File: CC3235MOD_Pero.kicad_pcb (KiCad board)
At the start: 2 copper layers, 37 parts, among them J1 USB_B_Mini, J2 JTAG/SWD, SW1 Reset, SW2 SW_DIP_x03, SW3 User IO, U1 TLV1117-33, U2 CP2102N-A01-GQFN24, U3 CC3235MODSF12MOBR

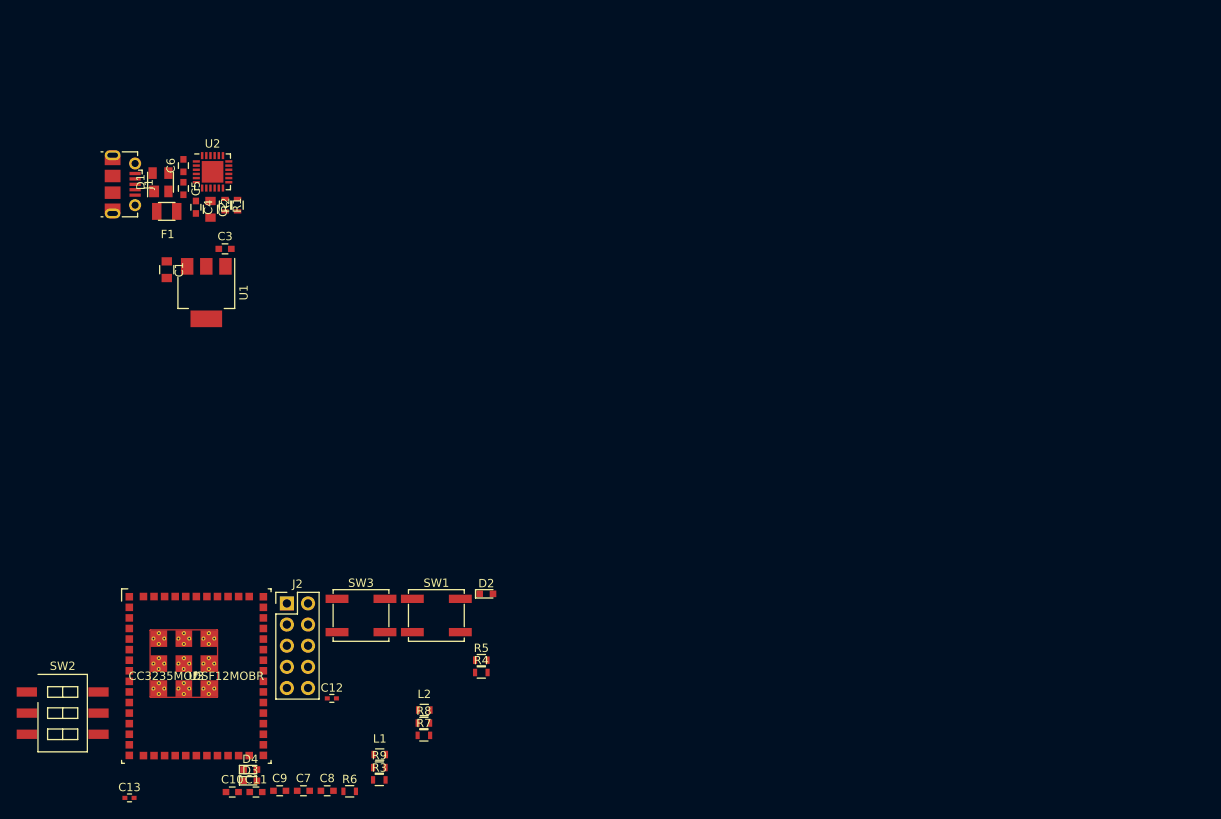
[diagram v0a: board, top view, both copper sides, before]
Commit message: antenna footprint done
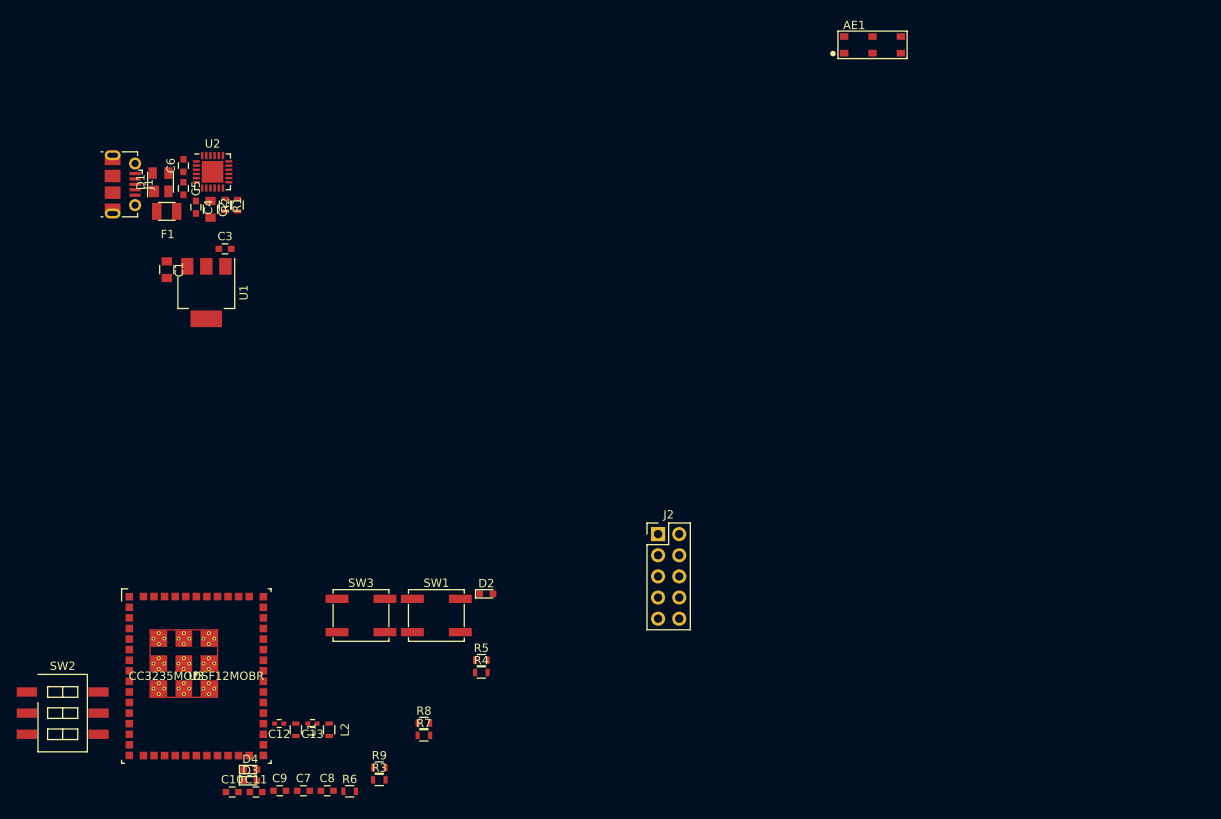
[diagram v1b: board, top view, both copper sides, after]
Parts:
- added AE1: Antenna, footprints:M830520, F.Cu at (148.8, 52.8)
- moved J2 45.3 mm to (123.0, 111.5)
- moved C13 23.7 mm to (81.5, 134.2), turned to 180 degrees
- moved L2 11.7 mm to (83.5, 135.0), turned to 270 degrees
- moved L1 10.5 mm to (79.5, 135.0), turned to 270 degrees
- moved C12 7.01 mm to (77.5, 134.2), turned to 180 degrees
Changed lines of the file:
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@@
     (tracks 0)
     (zones 0)
-    (modules 37)
+    (modules 38)
     (nets 72)
   )
@@
     (pad_to_mask_clearance 0.2)
     (aux_axis_origin 0 0)
-    (visible_elements FFFFFFFF)
+    (visible_elements 7FFFFFFF)
     (pcbplotparams
       (layerselection 0x010fc_ffffffff)
@@
     (add_net VBUS)
   )
+  (module footprints:M830520 (layer F.Cu)
+    (at 148.75 52.75)
+    (fp_text reference AE1 (at -2.2 -2.35) (layer F.SilkS)
+      (effects (font (size 1 1) (thickness 0.15)))
+    )
+    (fp_text value Antenna (at 0.7 2.5) (layer F.Fab)
+      (effects (font (size 1 1) (thickness 0.15)))
+    )
+    (fp_line (start -4 -1.5) (end 4 -1.5) (layer F.CrtYd) (width 0.1))
+    (fp_line (start 4 -1.5) (end 4 1.5) (layer F.CrtYd) (width 0.1))
+    (fp_line (start 4 1.5) (end -4 1.5) (layer F.CrtYd) (width 0.1))
+    (fp_line (start -4 1.5) (end -4 -1.5) (layer F.CrtYd) (width 0.1))
+    (fp_line (start -4.15 -1.65) (end 4.15 -1.65) (layer F.SilkS) (width 0.15))
+    (fp_line (start 4.15 -1.65) (end 4.15 1.6) (layer F.SilkS) (width 0.15))
+    (fp_line (start 4.15 1.6) (end 4.15 1.65) (layer F.SilkS) (width 0.15))
+    (fp_line (start 4.15 1.65) (end -4.15 1.65) (layer F.SilkS) (width 0.15))
+    (fp_line (start -4.15 1.65) (end -4.15 -1.65) (layer F.SilkS) (width 0.15))
+    (fp_circle (center -4.75 1.05) (end -4.5 1.05) (layer F.SilkS) (width 0.15))
+    (fp_circle (center -4.75 1.05) (end -4.65 1.05) (layer F.SilkS) (width 0.15))
+    (pad 1 smd rect (at -3.4 1) (size 1 0.8) (layers F.Cu F.Paste F.Mask)
+      (net 1 GND))
+    (pad 2 smd rect (at -3.4 -1) (size 1 0.8) (layers F.Cu F.Paste F.Mask)
+      (net 53 "Net-(AE1-Pad2)"))
+    (pad 3 smd rect (at 0 -1) (size 1 0.8) (layers F.Cu F.Paste F.Mask))
+    (pad 4 smd rect (at 3.4 -1) (size 1 0.8) (layers F.Cu F.Paste F.Mask))
+    (pad 5 smd rect (at 3.4 1) (size 1 0.8) (layers F.Cu F.Paste F.Mask))
+    (pad 6 smd rect (at 0 1) (size 1 0.8) (layers F.Cu F.Paste F.Mask))
+  )
   (module TO_SOT_Packages_SMD:SOT-143 (layer F.Cu)
     (at 63.25 69.25 90)
@@
   )
   (module Capacitors_SMD:C_0402 (layer F.Cu)
-    (at 59.525001 143.180001)
+    (at 81.5 134.25 180)
     (descr "Capacitor SMD 0402, reflow soldering, AVX (see smccp.pdf)")
     (tags "capacitor 0402")
     (attr smd)
-    (fp_text reference C13 (at 0 -1.27) (layer F.SilkS)
-      (effects (font (size 1 1) (thickness 0.15)))
-    )
-    (fp_text value C (at 0 1.27) (layer F.Fab)
-      (effects (font (size 1 1) (thickness 0.15)))
-    )
-    (fp_text user %R (at 0 -1.27) (layer F.Fab)
+    (fp_text reference C13 (at 0 -1.27 180) (layer F.SilkS)
+      (effects (font (size 1 1) (thickness 0.15)))
+    )
+    (fp_text value C (at 0 1.27 180) (layer F.Fab)
+      (effects (font (size 1 1) (thickness 0.15)))
+    )
+    (fp_text user %R (at 0 -1.27 180) (layer F.Fab)
       (effects (font (size 1 1) (thickness 0.15)))
     )
@@
     (fp_line (start 1 0.4) (end 1 -0.4) (layer F.CrtYd) (width 0.05))
     (fp_line (start 1 0.4) (end -1 0.4) (layer F.CrtYd) (width 0.05))
-    (pad 1 smd rect (at -0.55 0) (size 0.6 0.5) (layers F.Cu F.Paste F.Mask)
+    (pad 1 smd rect (at -0.55 0 180) (size 0.6 0.5) (layers F.Cu F.Paste F.Mask)
       (net 53 "Net-(AE1-Pad2)"))
-    (pad 2 smd rect (at 0.55 0) (size 0.6 0.5) (layers F.Cu F.Paste F.Mask)
+    (pad 2 smd rect (at 0.55 0 180) (size 0.6 0.5) (layers F.Cu F.Paste F.Mask)
       (net 54 "Net-(C12-Pad1)"))
     (model Capacitors_SMD.3dshapes/C_0402.wrl
@@
   )
   (module Capacitors_SMD:C_0402 (layer F.Cu)
-    (at 83.825001 131.230001)
+    (at 77.5 134.25 180)
     (descr "Capacitor SMD 0402, reflow soldering, AVX (see smccp.pdf)")
     (tags "capacitor 0402")
     (attr smd)
-    (fp_text reference C12 (at 0 -1.27) (layer F.SilkS)
-      (effects (font (size 1 1) (thickness 0.15)))
-    )
-    (fp_text value C (at 0 1.27) (layer F.Fab)
+    (fp_text reference C12 (at 0 -1.27 180) (layer F.SilkS)
+      (effects (font (size 1 1) (thickness 0.15)))
+    )
+    (fp_text value C (at 0 1.27 180) (layer F.Fab)
       (effects (font (size 1 1) (thickness 0.15)))
     )
@@
     (fp_line (start 0.5 0.25) (end -0.5 0.25) (layer F.Fab) (width 0.1))
     (fp_line (start -0.5 0.25) (end -0.5 -0.25) (layer F.Fab) (width 0.1))
-    (fp_text user %R (at 0 -1.27) (layer F.Fab)
-      (effects (font (size 1 1) (thickness 0.15)))
-    )
-    (pad 2 smd rect (at 0.55 0) (size 0.6 0.5) (layers F.Cu F.Paste F.Mask)
+    (fp_text user %R (at 0 -1.27 180) (layer F.Fab)
+      (effects (font (size 1 1) (thickness 0.15)))
+    )
+    (pad 2 smd rect (at 0.55 0 180) (size 0.6 0.5) (layers F.Cu F.Paste F.Mask)
       (net 23 /RF_OUT))
-    (pad 1 smd rect (at -0.55 0) (size 0.6 0.5) (layers F.Cu F.Paste F.Mask)
+    (pad 1 smd rect (at -0.55 0 180) (size 0.6 0.5) (layers F.Cu F.Paste F.Mask)
       (net 54 "Net-(C12-Pad1)"))
     (model Capacitors_SMD.3dshapes/C_0402.wrl
@@
   )
   (module Inductors_SMD:L_0603 (layer F.Cu)
-    (at 89.575001 137.975001)
+    (at 79.5 135 270)
     (descr "Resistor SMD 0603, reflow soldering, Vishay (see dcrcw.pdf)")
     (tags "resistor 0603")
     (attr smd)
-    (fp_text reference L1 (at 0 -1.9) (layer F.SilkS)
-      (effects (font (size 1 1) (thickness 0.15)))
-    )
-    (fp_text value L (at 0 1.9) (layer F.Fab)
-      (effects (font (size 1 1) (thickness 0.15)))
-    )
-    (fp_text user %R (at 0 0) (layer F.Fab)
+    (fp_text reference L1 (at 0 -1.9 270) (layer F.SilkS)
+      (effects (font (size 1 1) (thickness 0.15)))
+    )
+    (fp_text value L (at 0 1.9 270) (layer F.Fab)
+      (effects (font (size 1 1) (thickness 0.15)))
+    )
+    (fp_text user %R (at 0 0 270) (layer F.Fab)
       (effects (font (size 0.4 0.4) (thickness 0.075)))
     )
@@
     (fp_line (start 0.5 0.68) (end -0.5 0.68) (layer F.SilkS) (width 0.12))
     (fp_line (start -0.5 -0.68) (end 0.5 -0.68) (layer F.SilkS) (width 0.12))
-    (pad 1 smd rect (at -0.75 0) (size 0.5 0.9) (layers F.Cu F.Paste F.Mask)
+    (pad 1 smd rect (at -0.75 0 270) (size 0.5 0.9) (layers F.Cu F.Paste F.Mask)
       (net 54 "Net-(C12-Pad1)"))
-    (pad 2 smd rect (at 0.75 0) (size 0.5 0.9) (layers F.Cu F.Paste F.Mask)
+    (pad 2 smd rect (at 0.75 0 270) (size 0.5 0.9) (layers F.Cu F.Paste F.Mask)
       (net 1 GND))
     (model ${KISYS3DMOD}/Inductors_SMD.3dshapes/L_0603.wrl
@@
   )
   (module Inductors_SMD:L_0603 (layer F.Cu)
-    (at 94.925001 132.625001)
+    (at 83.5 135 270)
     (descr "Resistor SMD 0603, reflow soldering, Vishay (see dcrcw.pdf)")
     (tags "resistor 0603")
     (attr smd)
-    (fp_text reference L2 (at 0 -1.9) (layer F.SilkS)
-      (effects (font (size 1 1) (thickness 0.15)))
-    )
-    (fp_text value L (at 0 1.9) (layer F.Fab)
+    (fp_text reference L2 (at 0 -1.9 270) (layer F.SilkS)
+      (effects (font (size 1 1) (thickness 0.15)))
+    )
+    (fp_text value L (at 0 1.9 270) (layer F.Fab)
       (effects (font (size 1 1) (thickness 0.15)))
     )
@@
     (fp_line (start 0.8 0.4) (end -0.8 0.4) (layer F.Fab) (width 0.1))
     (fp_line (start -0.8 0.4) (end -0.8 -0.4) (layer F.Fab) (width 0.1))
-    (fp_text user %R (at 0 0) (layer F.Fab)
+    (fp_text user %R (at 0 0 270) (layer F.Fab)
       (effects (font (size 0.4 0.4) (thickness 0.075)))
     )
-    (pad 2 smd rect (at 0.75 0) (size 0.5 0.9) (layers F.Cu F.Paste F.Mask)
-      (net 1 GND))
-    (pad 1 smd rect (at -0.75 0) (size 0.5 0.9) (layers F.Cu F.Paste F.Mask)
+    (pad 2 smd rect (at 0.75 0 270) (size 0.5 0.9) (layers F.Cu F.Paste F.Mask)
+      (net 1 GND))
+    (pad 1 smd rect (at -0.75 0 270) (size 0.5 0.9) (layers F.Cu F.Paste F.Mask)
       (net 53 "Net-(AE1-Pad2)"))
     (model ${KISYS3DMOD}/Inductors_SMD.3dshapes/L_0603.wrl
@@
   )
   (module Pin_Headers:Pin_Header_Straight_2x05_Pitch2.54mm (layer F.Cu)
-    (at 78.425001 119.825001)
+    (at 123 111.5)
     (descr "Through hole straight pin header, 2x05, 2.54mm pitch, double rows")
     (tags "Through hole pin header THT 2x05 2.54mm double row")

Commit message: placement going
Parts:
- moved C10 86.1 mm to (121.7, 72.3)
- moved C9 84.8 mm to (121.7, 69.8)
- moved C11 83.3 mm to (121.7, 73.7)
- moved C8 83.3 mm to (121.7, 68.5)
- moved R6 76.2 mm to (121.7, 75.1), turned to 180 degrees
- moved C7 75.9 mm to (84.3, 66.5)
- moved SW2 74.3 mm to (113.0, 91.3), turned to 180 degrees
- moved D3 71.5 mm to (97.7, 73.7)
- moved R3 70.3 mm to (72.0, 72.9), turned to 90 degrees
- moved C12 68.7 mm to (121.2, 81.3)
- moved C13 68.7 mm to (125.2, 81.3)
- moved L1 68.7 mm to (123.2, 82.0)
- moved L2 68.7 mm to (127.2, 82.0)
- moved U3 68.7 mm to (111.2, 75.6)
- moved D4 67.4 mm to (97.7, 76.7)
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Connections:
- AE1 pad 1: GND -> Net-(AE1-Pad1)
- AE1 pad 2: Net-(AE1-Pad2) -> GND
- C13 pad 1: Net-(AE1-Pad2) -> Net-(AE1-Pad1)
- L2 pad 1: Net-(AE1-Pad2) -> Net-(AE1-Pad1)
- U3 pad 3: Net-(U3-Pad3) -> Net-(SW3-Pad2)
- U3 pad 44: Net-(SW3-Pad2) -> Net-(U3-Pad44)
- U3 pad 48: Net-(R9-Pad1) -> Net-(U3-Pad48)
- U3 pad 49: Net-(R8-Pad1) -> Net-(U3-Pad49)
- U3 pad 50: Net-(R7-Pad1) -> Net-(U3-Pad50)
- U3 pad 7: Net-(U3-Pad7) -> Net-(R8-Pad1)
- U3 pad 8: Net-(U3-Pad8) -> Net-(R7-Pad1)
- U3 pad 9: Net-(U3-Pad9) -> Net-(R9-Pad1)

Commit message: placement done
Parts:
- moved C6 78.9 mm to (138.3, 101.4), turned to 180 degrees
- moved U2 78.8 mm to (140.3, 106.8), turned to 270 degrees
- moved C7 78.2 mm to (145.5, 115.2), turned to 180 degrees
- moved C5 78.2 mm to (138.3, 103.0), turned to 180 degrees
- moved D1 77.3 mm to (130.8, 106.8), turned to 180 degrees
- moved J1 77.3 mm to (125.2, 107.4)
- moved R1 74.9 mm to (135.4, 102.9), turned to 180 degrees
- moved R3 74.8 mm to (141.2, 101.3), turned to 0 degrees
- moved C2 74.7 mm to (134.2, 106.8)
- moved C4 74.7 mm to (135.9, 106.4)
- moved F1 74.0 mm to (131.3, 103.4)
- moved R2 70.9 mm to (135.4, 101.5), turned to 180 degrees
- moved C3 61.8 mm to (141.1, 92.5), turned to 180 degrees
- moved U1 60.8 mm to (138.1, 96.9), turned to 0 degrees
- moved C1 60.3 mm to (132.6, 98.7), turned to 90 degrees
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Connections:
- D1 pad 2: VBUS -> /D-
- D1 pad 3: /D+ -> VBUS
- D1 pad 4: /D- -> /D+
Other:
- board outline added: 63.5 x 34.3 mm

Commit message: routing 90%
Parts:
- C12, C13: footprint Capacitors_SMD:C_0402 -> Capacitor_SMD:C_0603_1608Metric
- moved C7 9.91 mm to (155.4, 115.4)
- moved J2 9.91 mm to (155.1, 118.0)
- moved C4 8.27 mm to (141.5, 112.5)
- moved R3 8.27 mm to (146.8, 107.4)
- moved C1 8.27 mm to (138.2, 104.8)
- moved C2 8.27 mm to (139.8, 112.9)
- moved C3 8.27 mm to (146.7, 98.6)
- moved C5 8.27 mm to (143.9, 109.1)
- moved C6 8.27 mm to (143.9, 107.5)
- moved D1 8.27 mm to (136.4, 112.9)
- moved F1 8.27 mm to (136.9, 109.5)
- moved J1 8.27 mm to (130.7, 113.5)
- moved R1 8.27 mm to (141.0, 109.0)
- moved R2 8.27 mm to (141.0, 107.6)
- moved U2 8.27 mm to (145.9, 112.9)
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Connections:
- net Net-(AE1-Pad1) renamed /ANTENNA
- net Net-(C12-Pad1) renamed /PI
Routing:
- net +3V3: track 0.00 -> 110.1 mm, vias 0 -> 2
- net Net-(J2-Pad10): track 0.00 -> 61.4 mm, vias 0 -> 2
- net /RX: track 0.00 -> 43.2 mm, vias 0 -> 2
- net /TX: track 0.00 -> 40.6 mm, vias 0 -> 2
- net Net-(SW2-Pad6): track 0.00 -> 28.5 mm, vias 0 -> 2
- net Net-(J2-Pad8): track 0.00 -> 19.9 mm
- net /D-: track 0.00 -> 19.8 mm, vias 0 -> 2
- net /D+: track 0.00 -> 18.6 mm, vias 0 -> 2
- net Net-(J2-Pad4): track 0.00 -> 16.9 mm
- net Net-(J2-Pad2): track 0.00 -> 16.5 mm
- net Net-(J2-Pad6): track 0.00 -> 14.9 mm
- net Net-(R3-Pad2): track 0.00 -> 12.3 mm, vias 0 -> 2
- net Net-(SW2-Pad5): track 0.00 -> 11.3 mm
- net Net-(SW3-Pad2): track 0.00 -> 10.5 mm
- net GND: track 0.00 -> 9.53 mm, vias 0 -> 16
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- added copper zone on F.Cu, net +3V3
- added copper zone on F.Cu, net +5V
- added copper zone on B.Cu, net GND
- added copper zone on F.Cu, net GND
- added copper zone on F.Cu, net VBUS
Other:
- board size 63.5 x 34.3 mm -> 57.9 x 34.3 mm
- net class Default: via_dia 0.8 -> 0.5; via_drill 0.4 -> 0.3
- net class RF added: clearance 0.2, trace_width 0.82, via_dia 0.8, via_drill 0.3

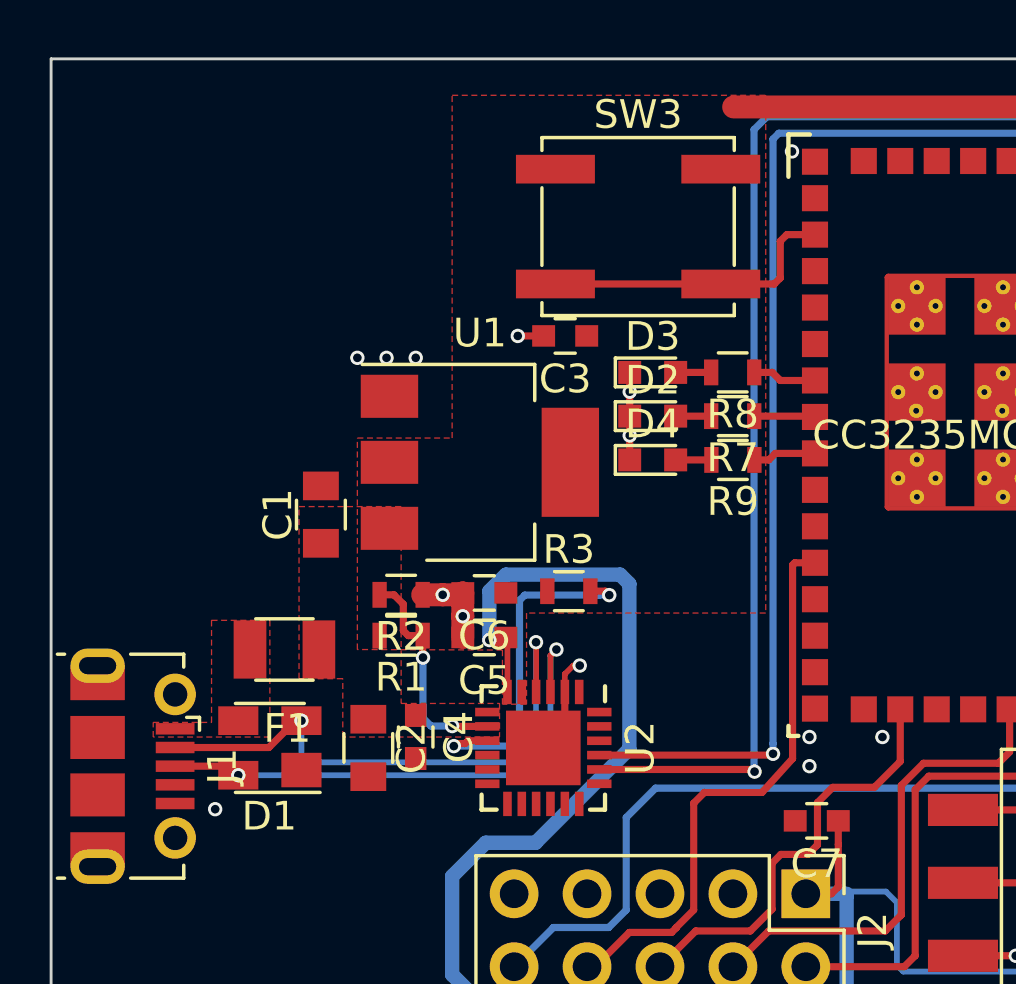
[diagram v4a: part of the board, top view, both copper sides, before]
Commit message: fixint antenna footprint
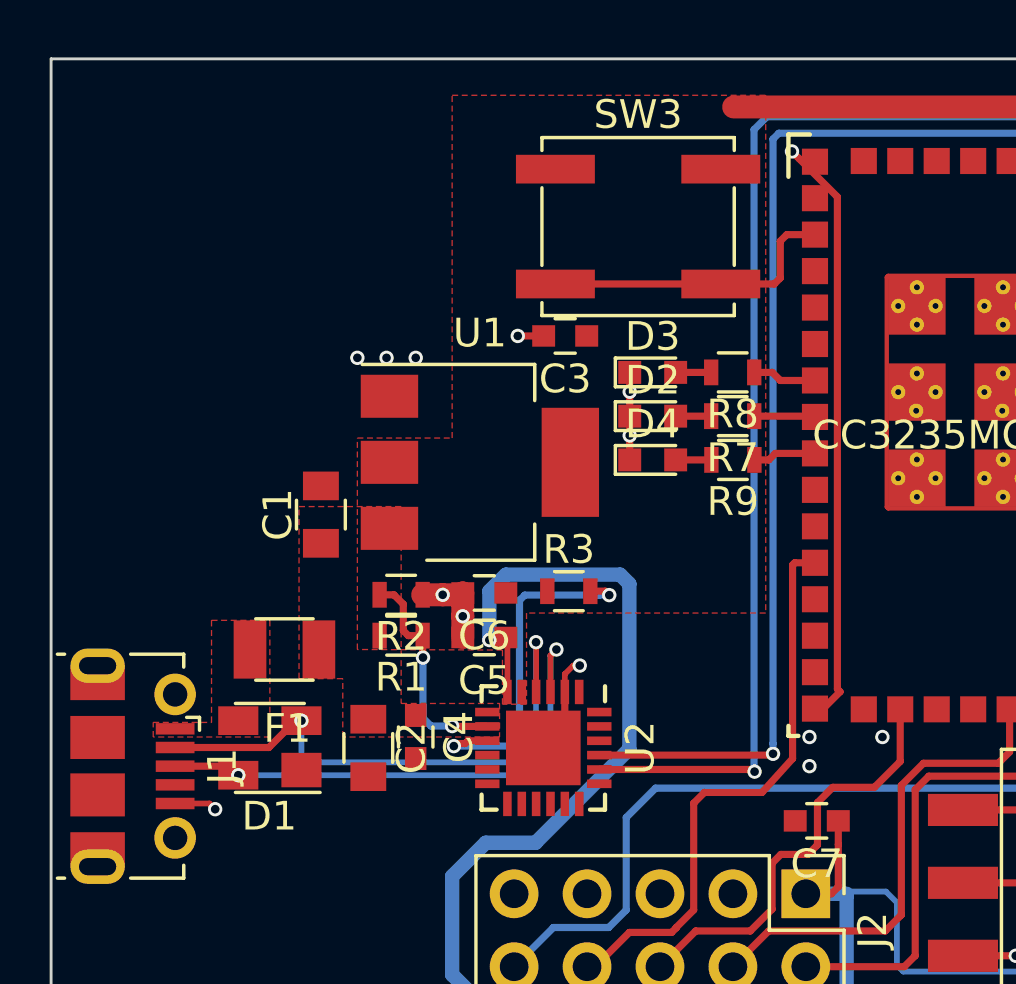
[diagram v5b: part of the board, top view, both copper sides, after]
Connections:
- U3 pad V: (no net) -> GND
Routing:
- net GND: track 9.53 -> 31.6 mm
